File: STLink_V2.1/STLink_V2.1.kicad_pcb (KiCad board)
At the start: 2 copper layers, 41 parts, among them J1 USB_C_Receptacle, J2 Conn_01x04_Pin, J3 Conn_01x04_Pin, J4 Conn_01x04_Pin, J5 Conn_01x05_Male, U1 STM32F103C8Tx, U2 RT9193-33GB, U3 ESP32-WROOM-32UE, Y1 Crystal_GND24_Small

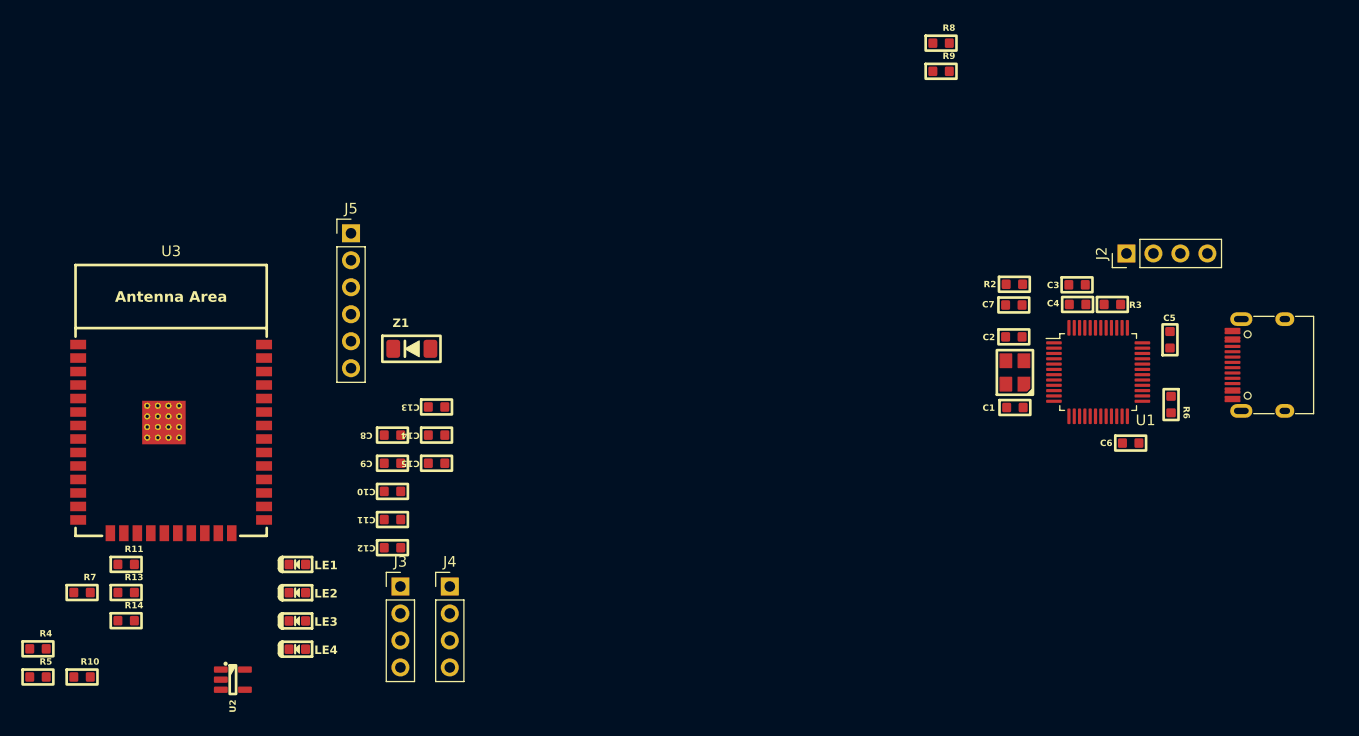
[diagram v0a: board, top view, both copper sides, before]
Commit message: Delete ESP32
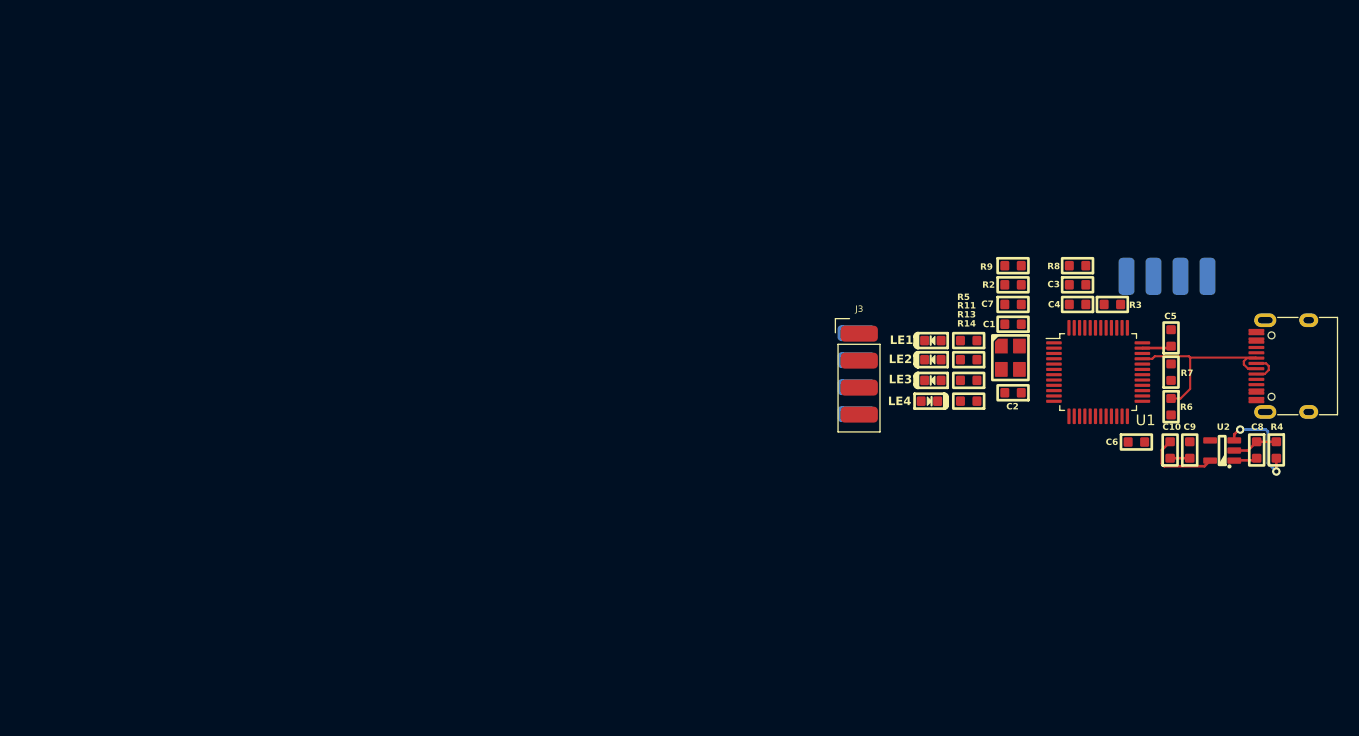
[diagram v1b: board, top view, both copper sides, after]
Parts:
- removed C11: 10uF, IVS_FOOTPRINTS:C_0603
- removed C12: 1uF, IVS_FOOTPRINTS:C_0603
- removed C13: 100nF, IVS_FOOTPRINTS:C_0603
- removed C14: 33pF, IVS_FOOTPRINTS:C_0603
- removed C15: 10pF, IVS_FOOTPRINTS:C_0603
- removed J5: Conn_01x05_Male, Connector_PinHeader_2.54mm:PinHeader_1x06_P2.54mm_Vertical
- removed R10: 100, IVS_FOOTPRINTS:R_0603
- removed U3: ESP32-WROOM-32UE, IVS_FOOTPRINTS:ESP32-WROOM-32E
- removed Z1: D_Zener, IVS_FOOTPRINTS:Package-Diode-D_MiniMELF
- J2, J4: footprint Connector_PinHeader_2.54mm:PinHeader_1x04_P2.54mm_Vertical -> IVS_FOOTPRINTS:Conn-Horz-SMD-4P-2.54mm-PinHeader; moved to B.Cu
- J3: footprint Connector_PinHeader_2.54mm:PinHeader_1x04_P2.54mm_Vertical -> IVS_FOOTPRINTS:Conn-Horz-SMD-4P-2.54mm-PinHeader
- moved R4 118.1 mm to (224.0, 83.4), turned to -90 degrees
- moved R7 104.6 mm to (214.1, 76.1), turned to 90 degrees
- moved U2 95.6 mm to (218.9, 83.5), turned to 180 degrees
- moved R5 93.2 mm to (195.0, 73.1), turned to 180 degrees
- moved R14 82.0 mm to (195.0, 78.8), turned to 180 degrees
- moved R13 81.8 mm to (195.0, 76.8), turned to 180 degrees
- moved R11 81.6 mm to (195.0, 74.9), turned to 180 degrees
- moved C8 81.4 mm to (222.1, 83.4), turned to -90 degrees
- moved C9 75.1 mm to (215.8, 83.4), turned to 90 degrees
- moved C10 73.3 mm to (214.0, 83.4), turned to 90 degrees
- moved LE3 64.0 mm to (191.6, 76.8)
- moved LE4 63.9 mm to (191.3, 78.8), turned to 180 degrees
- moved LE2 63.7 mm to (191.6, 74.9)
- moved LE1 63.4 mm to (191.6, 73.1)
- moved J3 49.3 mm to (184.7, 72.5)
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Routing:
- net /TYPE_C.D+: track 0.00 -> 19.0 mm
- net Net-(U2-EN): track 0.00 -> 9.33 mm, vias 0 -> 2
- net GND: track 0.00 -> 8.76 mm
- net +3V3: track 0.00 -> 7.24 mm
- net /TYPE_C.D-: track 0.00 -> 2.96 mm
- net +5V: track 0.00 -> 2.21 mm

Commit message: complete pcb layout
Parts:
- moved C2 0.42 mm to (198.8, 78.0)
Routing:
- net GND: track 8.76 -> 148.7 mm, vias 0 -> 1
- net +3V3: track 7.24 -> 136.3 mm, vias 0 -> 6
- net +5V: track 2.21 -> 60.9 mm, vias 0 -> 2
- net /T_SWDIO: track 0.00 -> 39.9 mm, vias 0 -> 2
- net /T_SWCLK: track 0.00 -> 35.7 mm
- net /T_TXD: track 0.00 -> 27.5 mm, vias 0 -> 2
- net /T_RXD: track 0.00 -> 26.3 mm, vias 0 -> 1
- net /RST: track 0.00 -> 14.3 mm
- net Net-(U1-PB12): track 0.00 -> 12.2 mm, vias 0 -> 2
- net /TYPE_C.D-: track 2.96 -> 14.1 mm, vias 0 -> 2
- net Net-(U1-PC14): track 0.00 -> 10.7 mm, vias 0 -> 2
- net Net-(U1-PC13): track 0.00 -> 10.6 mm, vias 0 -> 2
- net /ST_SWDIO: track 0.00 -> 9.92 mm, vias 0 -> 1
- net Net-(U1-PD0): track 0.00 -> 8.25 mm
- net Net-(U1-PD1): track 0.00 -> 5.79 mm
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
